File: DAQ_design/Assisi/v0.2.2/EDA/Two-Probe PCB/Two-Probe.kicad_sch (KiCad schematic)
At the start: 6 parts, among them J1 7-POS Plug Terminal, J2 Two-Probe Measurement, J3 7-POS Plug Terminal, J4 Four-Probe Measurement

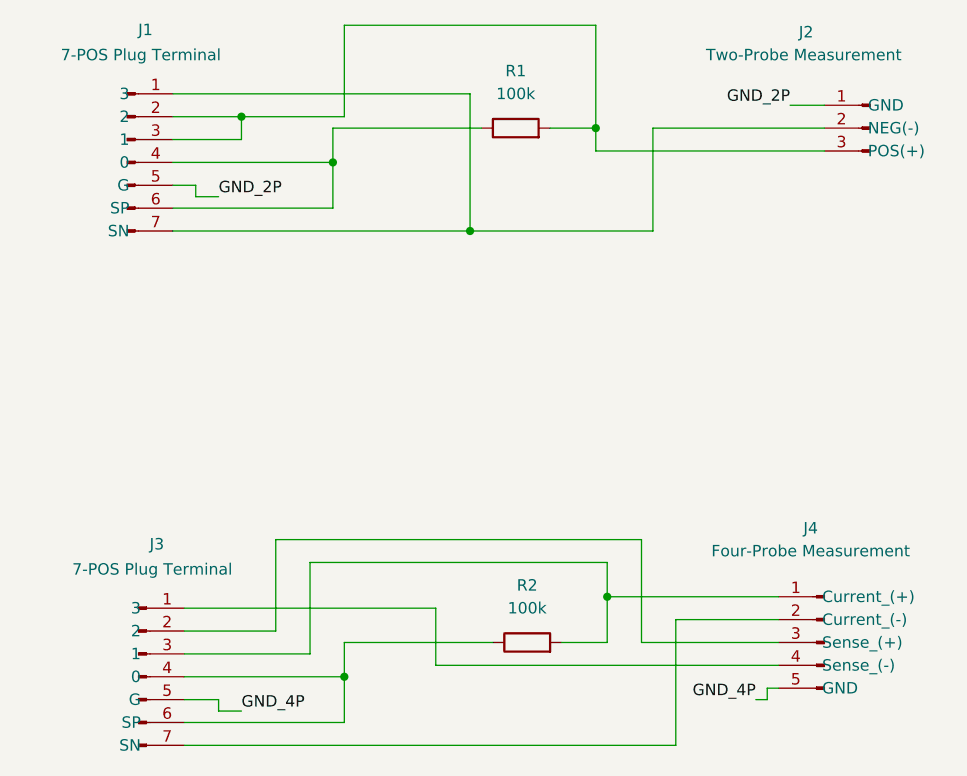
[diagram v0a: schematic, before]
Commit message: Separated PCBs: Two-Probe and Four-Probe
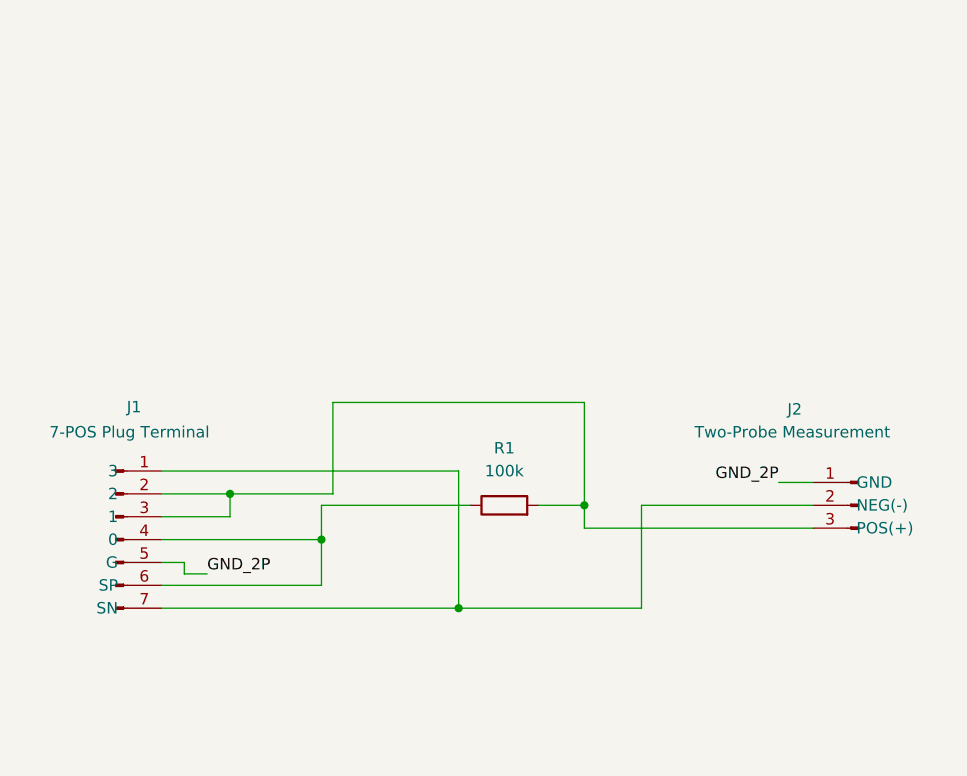
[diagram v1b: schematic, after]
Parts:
- removed J3: 7-POS Plug Terminal, EDA Footprint:PHOENIX_1786459, symbol Connector:Conn_01x07_Pin
- removed J4: Four-Probe Measurement, Connector_Phoenix_MSTB:PhoenixContact_MSTBA_2,5_5-G-5,08_1x05_P5.08mm_Horizontal, symbol Connector:Conn_01x05_Pin
- removed R2: 100k, Resistor_THT:R_Axial_DIN0207_L6.3mm_D2.5mm_P10.16mm_Horizontal, symbol Device:R
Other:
- moved on the sheet: J1, J2, R1
